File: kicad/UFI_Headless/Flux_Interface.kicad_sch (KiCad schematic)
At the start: 36 parts, among them Q5 2N7002, U14 74LVC1G32GW, U22 TS5A3166DBVR, U6 SN74LS07D, U7 SN74LS07D, U8 74LVC14AD

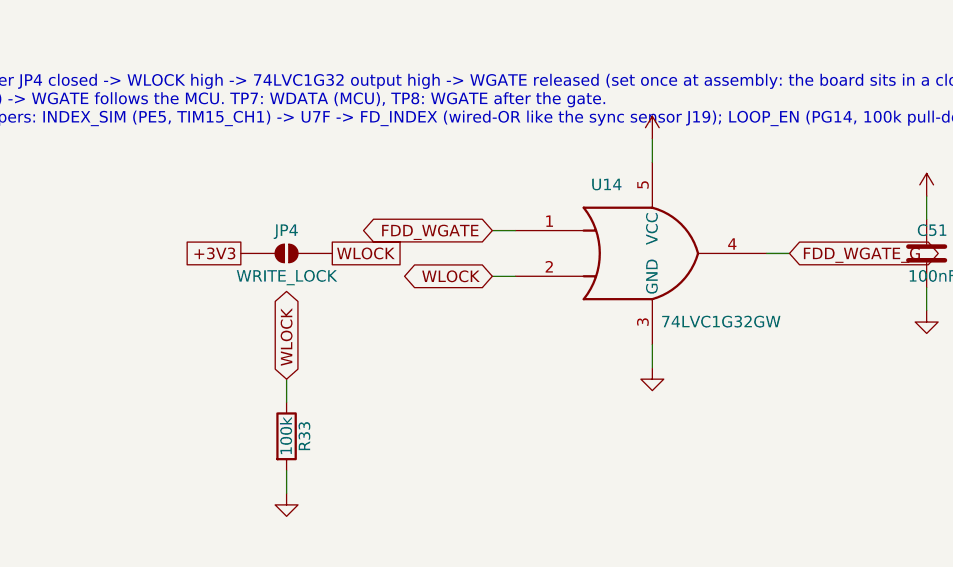
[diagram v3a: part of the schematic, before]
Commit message: KiCad v0.7 rework, stage A9b (owner definition of 2026-10-24): write protection is on by default and INDEX also reaches TIM2_CH4 - Flux_Interface: R33 becomes a 10k pull-up from WLOCK_HW to +3V3 (C25804; was 100k to GND), the solder jumper JP4 is gone, U14 74LVC1G32 -> 74LVC1G332 3-input OR (TI SN74LVC1G332DCKR C2865081, SC-70-6; alternative Nexperia 74LVC1G332GW C548342) with FDD_WGATE, WLOCK_HW and WLOCK_FW as inputs and FDD_WGATE_G as output, R131 100k pull-up on WLOCK_FW so the gate is closed through reset and boot; MCU_Core: U5 PE4 = WLOCK_FW (output), PE6 = WREN_SENSE through R130 470 R from WLOCK_HW, PB11 = FDD_INDEX (TIM2_CH4, AF1 verified against the STM32H723ZG pin database: PB11 TIM2 CH4 AF1, PE4/PE6 plain GPIO, PC14/PC15 OSC32), no-connect flags on PE6/PB11 removed; front header J12 pin 12 = WLOCK_HW (switch SCHREIBEN to GND = write enabled, cable off = locked), pin 10 = FRONT_WRLED (+3V3 through R128 1k, LED anode; LED cathode on pin 12 lights "write enabled"), D28/D29 PESD3V3L1BA on both, even pins 2-8 stay GND; J12 note updated. Firmware in the same commit: board.h/board_headless.c PE4 driven high before it becomes an output (no low glitch into the OR gate), PE6 input, PB11 AF1 input (the capture code keeps using CH2 on PA1 - CH4 is wired for the pulse-width measurement later), ufi_board.c ufi_board_jumper_locked() reads PE6 on board_rev >= 10 and PE4 on v0.x, new ufi_board_write_enable(on) drives WLOCK_FW low only while a write runs (on v0.x it restores PE4 as the jumper input once), ufi_write.c calls it after the lock checks and in write_finish (two hunks staged from the owner's working copy); protocol doc: board_status flags bit 0 explained for v1.0. ERC over the whole project 0 errors / 0 warnings (build/erc.rpt); ARM build and offline gate as reported in the stage log. PLAN.md A9 row (A9b done, A9c soft start + RTC open), kicad README (A9b row, GPIO table PE4/PE6/PB11). The PCB follows in B3.
Claude-Session: https://claude.ai/code/session_014Mdzr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
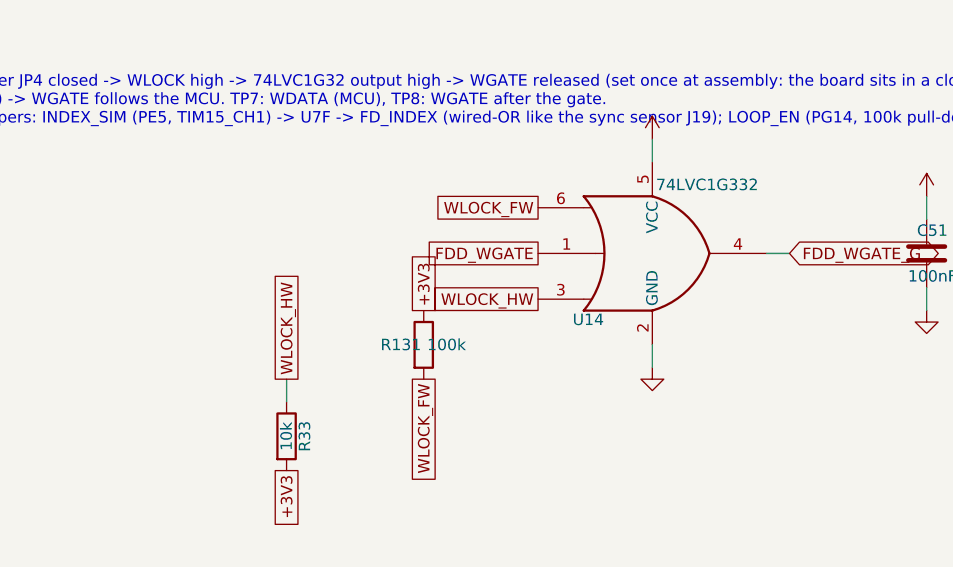
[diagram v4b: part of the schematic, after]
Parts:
- removed JP4: WRITE_LOCK, Jumper:SolderJumper-2_P1.3mm_Open_RoundedPad1.0x1.5mm, symbol Jumper:SolderJumper_2_Open
- removed U14: 74LVC1G32GW, Package_TO_SOT_SMD:SOT-353_SC-70-5, symbol 74xGxx:74LVC1G32
- added R131: 100k, Resistor_SMD:R_0603_1608Metric, symbol Device:R
- added U14: 74LVC1G332, Package_TO_SOT_SMD:SOT-363_SC-70-6, symbol 74xGxx:74LVC1G332
- R33: value 100k -> 10k; LCSC C25803 -> C25804; Note (none) -> pull-up: WLOCK_HW high = write locked by default; the front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
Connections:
- net +3V3: now also R33.2, R131.1, U14.5 (VCC)
- net FDD_WGATE: now also U14.1
- net FDD_WGATE_G: now also U14.4
- net GND: now also U14.2 (GND); no longer R33.2
- net WLOCK renamed WLOCK_HW
- net WLOCK_HW: now also U14.3
- new net WLOCK_FW: R131.2, U14.6

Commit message: KiCad v0.7 rework, stage A11a (owner's device-comparison list M1, M4, M6): write lock gates both write requests, terminations on FDD_5V, JP2 gone - Flux_Interface: U14 becomes a 74LVC1G32 (Diodes 74LVC1G32SE-7 C460530, SOT-353; was the 74LVC1G332 of A9b) forming the global net LOCK = WLOCK_HW or WLOCK_FW; new U30 74LVC2G32 (Nexperia 74LVC2G32DP,125 C548635, TSSOP-8; single-unit project symbol UFI_Headless:74LVC2G32 because the KiCad multi-unit symbol does not work with the MCP placement, pinout 1 1A 2 1B 3 2Y 4 GND 5 2A 6 2B 7 1Y 8 VCC from the datasheet family) gates FDD_WGATE -> FDD_WGATE_G (U7 pin 3, TP8) and APL_WRREQ -> APL_WRREQ_G (new global net to U16 2A2 on Apple_Port, the MCU-side pull-up RN10 stays on APL_WRREQ), C84 100 nF; both requests are active low, LOCK high forces them inactive, so the Apple write request no longer bypasses the lock (netlist: LOCK = U14.4 U30.2 U30.6, APL_WRREQ_G = U16.13 U30.3, FDD_WGATE_G = U7.3 U30.7 TP8.1). M4: R75-R91 (Flux_Interface) and R97-R99 (FDD_Connectors, same reason) pull up to FDD_5V instead of +5V, R92-R96 on the IEC bus stay at +5V. M6: JP2 with its GND symbol and labels removed, J6 pin 3 is GND. Note on the sheet. ERC over the whole project 0 errors / 0 warnings (build/erc.rpt). No firmware change (WLOCK_FW/WLOCK_HW semantics unchanged). PLAN.md A11a done, kicad README A11a row. PCB follows in B3.
Claude-Session: https://claude.ai/code/session_014MdzrcyXuayppPHbfEjUrw
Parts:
- removed U14: 74LVC1G332, Package_TO_SOT_SMD:SOT-363_SC-70-6, symbol 74xGxx:74LVC1G332
- added C84: 100nF, Capacitor_SMD:C_0603_1608Metric, symbol Device:C
- added U14: 74LVC1G32, Package_TO_SOT_SMD:SOT-353_SC-70-5, symbol 74xGxx:74LVC1G32
- added U30: 74LVC2G32, Package_SO:TSSOP-8_3x3mm_P0.65mm, symbol UFI_Headless:74LVC2G32
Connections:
- net +3V3: now also C84.1, U14.5 (VCC), U30.8 (VCC)
- net +5V: no longer R75.2, R76.2, R77.2, R78.2, R79.2, R80.2, R81.2, R82.2, R83.2, R84.2, R85.2, R86.2, R87.2, R88.2, R89.2, R90.2, R91.2
- net FDD_WGATE: now also U30.1 (1A)
- net FDD_WGATE_G: now also U30.7 (1Y)
- net GND: now also C84.2, U14.3 (GND), U30.4 (GND)
- net WLOCK_FW: now also U14.2
- net WLOCK_HW: now also U14.1
- new net APL_WRREQ: U30.5 (2A)
- new net APL_WRREQ_G: U30.3 (2Y)
- new net FDD_5V: R75.2, R76.2, R77.2, R78.2, R79.2, R80.2, R81.2, R82.2, R83.2, R84.2, R85.2, R86.2, R87.2, R88.2, R89.2, R90.2, R91.2
- new net LOCK: U14.4, U30.2 (1B), U30.6 (2B)
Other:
- note added: "A11a (24.10.2026, owner list M1/M4/M6): U14 74LVC1G32 forms LOCK = WLOCK_HW or WLOCK_FW (both high = locked; reset and cable-off states are locked). U30 74LVC2G32 gates the two write requests with LOCK: FDD_WGATE -> FDD_WGATE_G (U7 -> J6/J7 pin 24) and APL_WRREQ -> APL_WRREQ_G (U16 2A2 -> J14 pin 10). Both are active low, LOCK high forces them inactive. Replaces the 3-input OR of A9b; a later Mac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"

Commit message: KiCad v0.7 rework, stage A11b (owner's device-comparison list M3, BSS138DW confirmed 2026-10-25): Shugart/Amiga bus outputs through MOSFETs instead of the LS07 - Flux_Interface: U6/U7 SN74LS07 (with C40/C41 and their power symbols) removed, six dual N-MOSFETs Q6-Q11 Diodes BSS138DW-7-F (C154900, SOT-363, JLC stock 141516; single-unit project symbol UFI_Headless:BSS138DW with the pinout from the datasheet top view 1 S2, 2 G2, 3 D1, 4 S1, 5 G1, 6 D2; VGS(th) 0.5-1.5 V, RDS(on) 3.5 Ohm max at 10 V, ID 200 mA; the 2N7002DW of the plan was dropped because its 7.5 Ohm at 5 V would give up to 0.4 V at 40 mA from a 3.3 V gate) give the twelve open-drain channels Q6 MOTOR_A/MOTOR_B, Q7 DRVSEL_A/DRVSEL_B, Q8 STEP/DIR, Q9 SIDE/WGATE_G, Q10 WDATA/DENSITY, Q11 DRATE/INDEX_SIM (drain on FD_*, gate on FDD_*/INDEX_SIM, source GND), R144-R155 100k (C25803) gate pull-downs keep every line released through reset; the IEC driver U9 stays an LS07 per the owner (three 1k pull-ups = 15 mA within its 16 mA / 0.4 V spec). Netlist compared against the state before A11a: only the intended pins changed. ERC over the whole project 0 errors / 0 warnings (build/erc.rpt). Firmware in the same commit: board.h bus_out()/bus_out_state() invert on v1.0 for every bus output not on GPIOD (IEC keeps the LS07 polarity) via the new flag board_fdd_mosfet, board_headless.c sets the flag from ufi_board_rev() at the start of board_gpio_init() (ADC self-initialises) and latches the released level low for PE7-PE15, PF11, PA6 and PE5 on v1.0 before switching them to outputs (the 100k pull-downs hold them released until then, floating LS07 inputs on v0.x likewise), ufi_diag.c TIM15_CH1 INDEX_SIM polarity high / idle reset and sim_pin() release level low on v1.0, ufi_write.c TIM3_CH1 WDATA polarity high on v1.0 (one hunk in the owner's working copy), ufi_debug.c fdd_outputs reporting follows through bus_out_state(); v0.x boards behave exactly as before. Protocol doc (one hunk): INDEX_SIM bullet names the MOSFET dri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
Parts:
- removed C40, C41: 100nF, Capacitor_SMD:C_0603_1608Metric, symbol Device:C
- removed U6, U7: SN74LS07D, Package_SO:SOIC-14_3.9x8.7mm_P1.27mm, symbol 74xx:74LS07
- added Q10, Q11, Q6, Q7, Q8, Q9: BSS138DW, Package_TO_SOT_SMD:SOT-363_SC-70-6, symbol UFI_Headless:BSS138DW
- added R144, R145, R146, R147, R148, R149, R150, R151, R152, R153, R154, R155: 100k, Resistor_SMD:R_0603_1608Metric, symbol Device:R
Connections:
- net FDD_DENSITY: now also Q10.2 (G2), R153.1
- net FDD_DIR: now also Q8.2 (G2), R149.1
- net FDD_DRATE: now also Q11.5 (G1), R154.1
- net FDD_DRVSEL_A: now also Q7.5 (G1), R146.1
- net FDD_DRVSEL_B: now also Q7.2 (G2), R147.1
- net FDD_MOTOR_A: now also Q6.5 (G1), R144.1
- net FDD_MOTOR_B: now also Q6.2 (G2), R145.1
- net FDD_SIDE: now also Q9.5 (G1), R150.1
- net FDD_STEP: now also Q8.5 (G1), R148.1
- net FDD_WDATA: now also Q10.5 (G1), R152.1
- net FDD_WGATE_G: now also Q9.2 (G2), R151.1
- net FD_DENSITY: now also Q10.6 (D2)
- net FD_DIR: now also Q8.6 (D2)
- net FD_DRATE: now also Q11.3 (D1)
- net FD_DRVSEL_A: now also Q7.3 (D1)
- net FD_DRVSEL_B: now also Q7.6 (D2)
- net FD_INDEX: now also Q11.6 (D2)
- net FD_MOTOR_A: now also Q6.3 (D1)
- net FD_MOTOR_B: now also Q6.6 (D2)
- net FD_SIDE: now also Q9.3 (D1)
- net FD_STEP: now also Q8.3 (D1)
- net FD_WDATA: now also Q10.3 (D1)
- net FD_WGATE: now also Q9.6 (D2)
- net GND: now also Q10.1 (S2), Q10.4 (S1), Q11.1 (S2), Q11.4 (S1), Q6.1 (S2), Q6.4 (S1), Q7.1 (S2), Q7.4 (S1), Q8.1 (S2), Q8.4 (S1), Q9.1 (S2), Q9.4 (S1), R144.2, R145.2, R146.2, R147.2, R148.2, R149.2, R150.2, R151.2, R152.2, R153.2, R154.2, R155.2
- net INDEX_SIM: now also Q11.2 (G2), R155.1
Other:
- note added: "A11b (25.10.2026, owner list M3): the LS07 drivers U6/U7 are replaced by six dual N-MOSFETs Q6-Q11 (Diodes BSS138DW-7-F, VGS(th) <= 1.5 V, RDS(on) <= 3.5 Ohm at 10 V): gate = MCU line FDD_*, drain = bus line FD_* (open drain, pulled up by the 1k terminations on FDD_5V), source = GND; R144-R155 100k gate pull-downs keep every line released through reset. An LS07 guarantees 0.4 V only up to 16 mA, 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"

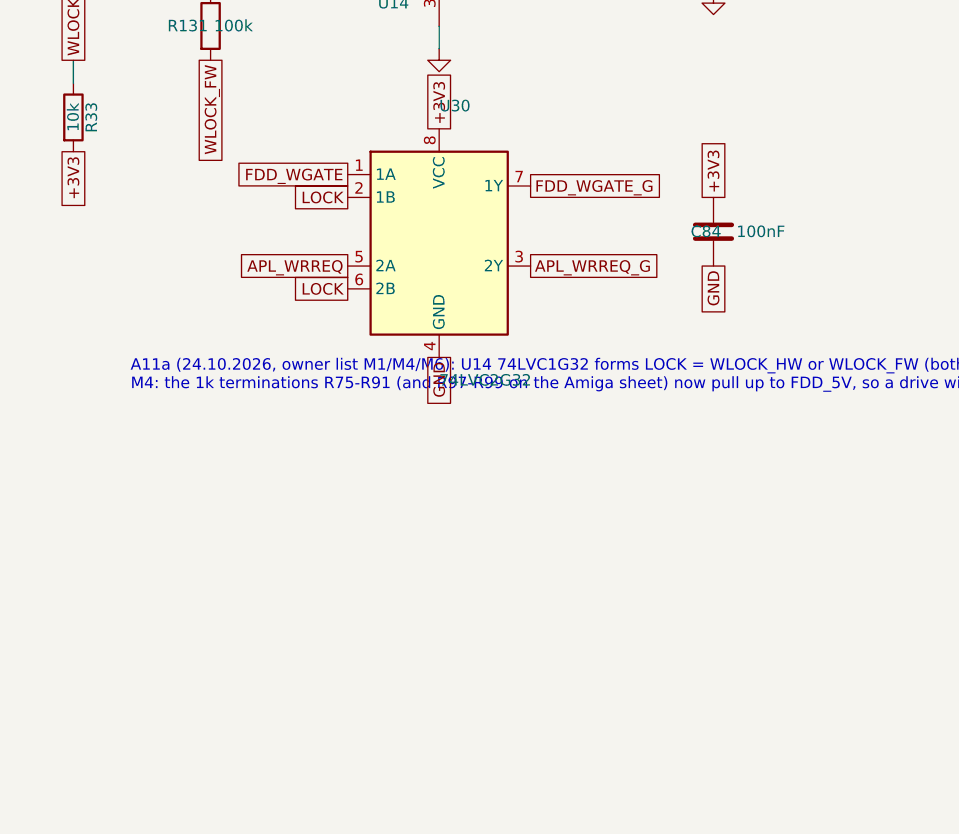
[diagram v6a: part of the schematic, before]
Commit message: KiCad v0.7 rework, stage A11f (fixes from the A8 review, owner decisions of 2026-10-25): F1 - the write gate is now hard-gated by a NOR instead of the A11a OR that had driven the MOSFET gate the wrong way since A11b: new U31 74LVC1G02 (MDD 74LVC1G02GW C52953351, SOT-353) on Flux_Interface forms Q9 gate = NOR(WGATE_n, LOCK), PE14 becomes WGATE_n (active low on every board revision again) with R167 10k pull-up to +3V3 so reset and boot leave the gate released, C88 100 nF; U30 gate 1 retired (1A/1B on GND, 1Y no-connect), gate 2 still gates APL_WRREQ with LOCK; netlist: FDD_WGATE = U5.67 R167 U31.1 J21.7, FDD_WGATE_G = U31.4 Q9.2 R151 TP8, LOCK = U14.4 U30.6 U31.2. Firmware in the same commit: board.h bus_out_inverted() excludes PE14, board_headless.c latches PE14 high at start-up; truth table for every MOSFET-driven line (reset / idle / active) recorded in PLAN.md, measurement point "J6 pin 24 stays high with the lock set during a read" in the README row, self-test item planned for A10; protocol doc (one hunk in the board_status bit 0 note). R1: D30 removed, SYNC_5V protected by the 5 V channel IO3 of D31 ESDA6V1-5SC6, J19 becomes a keyed JST B3B-XH-A (C144394). R2: J20 GUARD becomes JST B4B-XH-A (C144395) with D32-D34 PESD3V3L1BA (C51450) on GUARD_OFF_J/ERR5_J/ERR12_J; note that the Guard board v0.2 gets a JST XH J3 too. R3: flippy divider kept at 2.4k/2.4k (C22940, Greaseweazle V4.1 compatible), JP7 default GND. ERC over the whole project 0 errors / 0 warnings (build/erc.rpt). ARM build 0 warnings; offline gate as reported in the stage log. PLAN.md (A11f, polarity table), kicad README (A11f row). PCB follows in B3.
Claude-Session: https://claude.ai/code/session_014MdzrcyXuayppPHbfEjUrw
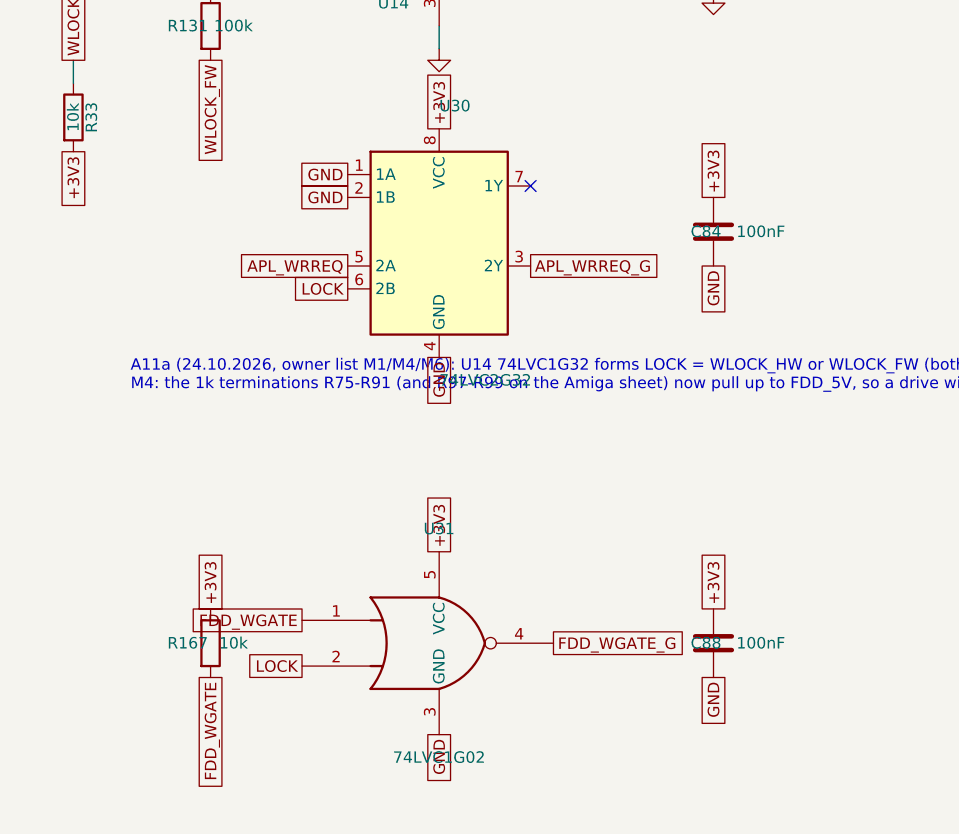
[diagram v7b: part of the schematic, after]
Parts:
- added C88: 100nF, Capacitor_SMD:C_0603_1608Metric, symbol Device:C
- added R167: 10k, Resistor_SMD:R_0603_1608Metric, symbol Device:R
- added U31: 74LVC1G02, Package_TO_SOT_SMD:SOT-353_SC-70-5, symbol 74xGxx:74LVC1G02
- U30: MPN Nexperia 74LVC2G32DP,125 (dual 2-input OR: FDD_WGATE|LOCK -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 -> Nexperia 74LVC2G32DP,125 - gate 1 retired in A11f (inputs o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
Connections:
- net +3V3: now also C88.1, R167.1, U31.5 (VCC)
- net FDD_WGATE: now also R167.2, U31.1; no longer U30.1 (1A)
- net FDD_WGATE_G: now also U31.4; no longer U30.7 (1Y)
- net GND: now also U30.1 (1A), U30.2 (1B), C88.2, U31.3 (GND)
- net LOCK: now also U31.2; no longer U30.2 (1B)
- no-connect marks 0 -> 1
